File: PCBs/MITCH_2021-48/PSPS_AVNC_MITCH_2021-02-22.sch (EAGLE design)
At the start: 54 parts, among them J1 A-1JB, U0-C STM32F411CEUX, U1-S ICM-20948, U11-S SN74LV1T34, U12-S SN74LV1T34, U13-S SN74LV1T34, U14-S SN74LV1T34, U14-S1 SN74LV1T34, U14-S2 SN74LV1T34, U2-S MMA1211KEG

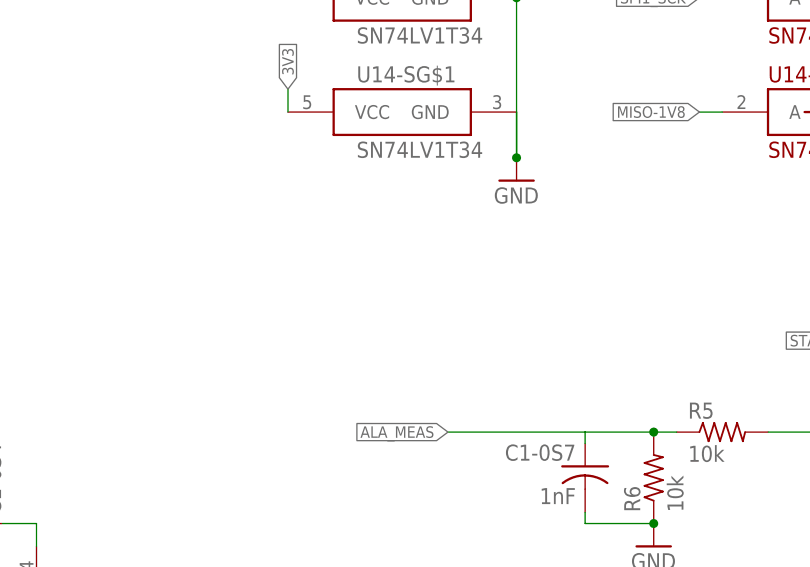
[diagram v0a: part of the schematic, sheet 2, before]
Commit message: Updated silk screen
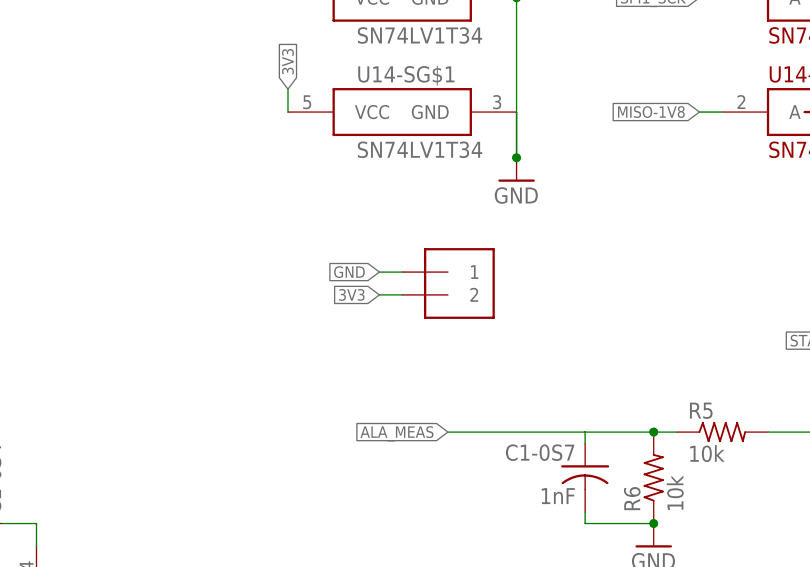
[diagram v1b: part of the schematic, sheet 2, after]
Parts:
- added J2: 1X2-3.5MM, adafruit:1X2-3.5MM
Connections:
- net 3V3: now also J2.2
- net GND: now also J2.1
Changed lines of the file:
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@@
 <part name="C5-0C1" library="resistor" library_urn="urn:adsk.eagle:library:348" deviceset="C-US" device="C0805" package3d_urn="urn:adsk.eagle:package:23617/2" value="0.1uF"/>
 <part name="GND21" library="supply1" library_urn="urn:adsk.eagle:library:371" deviceset="GND" device=""/>
+<part name="J2" library="adafruit" library_urn="urn:adsk.eagle:library:420" deviceset="1X2" device="-3.5MM" package3d_urn="urn:adsk.eagle:package:6240635/1"/>
 </parts>
 <sheets>
@@
 <attribute name="VALUE" x="180.34" y="27.94" size="1.778" layer="96"/>
 </instance>
+<instance part="J2" gate="G$1" x="91.44" y="50.8" smashed="yes"/>
 </instances>
 <busses>
@@
 <wire x1="96.52" y1="162.56" x2="96.52" y2="165.1" width="0.1524" layer="91"/>
 <label x="96.52" y="165.1" size="1.27" layer="95" rot="R90" xref="yes"/>
+</segment>
+<segment>
+<pinref part="J2" gate="G$1" pin="2"/>
+<wire x1="86.36" y1="50.8" x2="83.82" y2="50.8" width="0.1524" layer="91"/>
+<label x="83.82" y="50.8" size="1.27" layer="95" rot="R180" xref="yes"/>
 </segment>
 </net>
@@
 <pinref part="GND20" gate="1" pin="GND"/>
 </segment>
-</net>
+<segment>
+<pinref part="J2" gate="G$1" pin="1"/>
+<wire x1="86.36" y1="53.34" x2="83.82" y2="53.34" width="0.1524" layer="91"/>
+<label x="83.82" y="53.34" size="1.27" layer="95" rot="R180" xref="yes"/>
+</segment>
+</net>

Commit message: Continued refining MITCH 2021.0
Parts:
- added R9: (no value), resistor:R-US_R0805
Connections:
- net BUTTON_IN: now also R9.1
- net GND: now also R9.2
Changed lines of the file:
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@@
 <part name="GND21" library="supply1" library_urn="urn:adsk.eagle:library:371" deviceset="GND" device=""/>
 <part name="J2" library="adafruit" library_urn="urn:adsk.eagle:library:420" deviceset="1X2" device="-3.5MM" package3d_urn="urn:adsk.eagle:package:6240635/1"/>
+<part name="R9" library="resistor" library_urn="urn:adsk.eagle:library:348" deviceset="R-US_" device="R0805" package3d_urn="urn:adsk.eagle:package:23553/2"/>
 </parts>
 <sheets>
@@
 <instance part="GND21" gate="1" x="27.94" y="-96.52" smashed="yes">
 <attribute name="VALUE" x="25.4" y="-99.06" size="1.778" layer="96"/>
+</instance>
+<instance part="R9" gate="G$1" x="68.58" y="-68.58" smashed="yes">
+<attribute name="NAME" x="64.77" y="-67.0814" size="1.778" layer="95"/>
+<attribute name="VALUE" x="64.77" y="-71.882" size="1.778" layer="96"/>
 </instance>
 </instances>
@@
 <pinref part="GND21" gate="1" pin="GND"/>
 </segment>
+<segment>
+<pinref part="R9" gate="G$1" pin="2"/>
+<wire x1="73.66" y1="-68.58" x2="76.2" y2="-68.58" width="0.1524" layer="91"/>
+<label x="76.2" y="-68.58" size="1.27" layer="95" xref="yes"/>
+</segment>
 </net>
 <net name="SWDIO" class="0">
@@
 <label x="58.42" y="-17.78" size="1.27" layer="95" xref="yes"/>
 </segment>
-</net>
+<segment>
+<pinref part="R9" gate="G$1" pin="1"/>
+<wire x1="63.5" y1="-68.58" x2="60.96" y2="-68.58" width="0.1524" layer="91"/>
+<label x="60.96" y="-68.58" size="1.27" layer="95" rot="R180" xref="yes"/>
+</segment>
+</net>
